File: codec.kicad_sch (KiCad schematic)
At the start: 0 parts

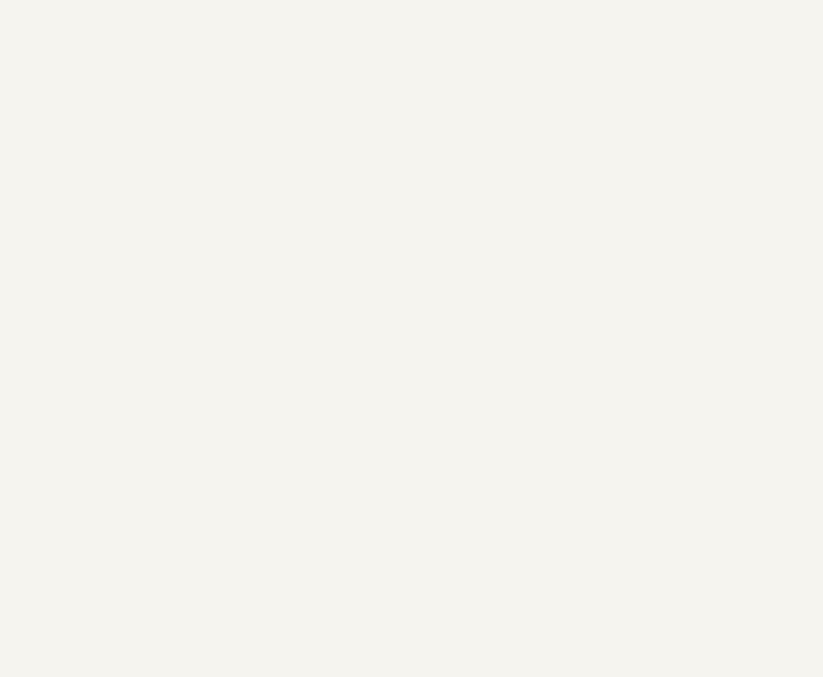
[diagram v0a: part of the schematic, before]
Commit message: Add codec ic
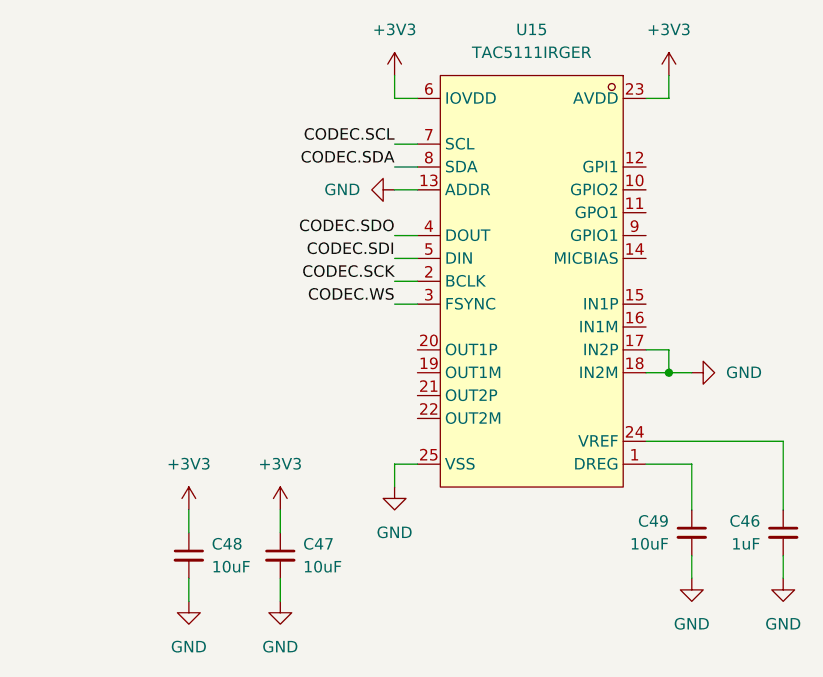
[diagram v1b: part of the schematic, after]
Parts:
- added C46: 1uF, Capacitor_SMD:C_0402_1005Metric, symbol Device:C_Small
- added C47, C48, C49: 10uF, Capacitor_SMD:C_0603_1608Metric, symbol Device:C_Small
- added U15: TAC5111IRGER, custom:VQFN-24_L4.0-W4.0-P0.50-BL-EP2.1_1, symbol custom:TAC5111IRGER
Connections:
- net CODEC.SCK: now also U15.2 (BCLK)
- net CODEC.SCL: now also U15.7 (SCL)
- net CODEC.SDA: now also U15.8 (SDA)
- net CODEC.SDI: now also U15.5 (DIN)
- net CODEC.SDO: now also U15.4 (DOUT)
- net CODEC.WS: now also U15.3 (FSYNC)
- new net: C49.1, U15.1 (DREG)
- new net: C46.1, U15.24 (VREF)
- new net +3V3: C47.1, C48.1, U15.23 (AVDD), U15.6 (IOVDD)
- new net GND: C46.2, C47.2, C48.2, C49.2, U15.13 (ADDR), U15.17 (IN2P), U15.18 (IN2M), U15.25 (VSS), U15.A1 (VSS), U15.A2 (VSS), U15.A3 (VSS), U15.A4 (VSS)

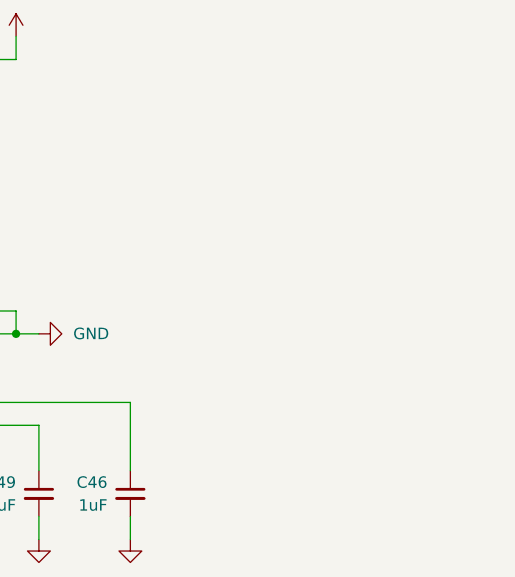
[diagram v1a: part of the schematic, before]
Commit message: Add preamp opamp library
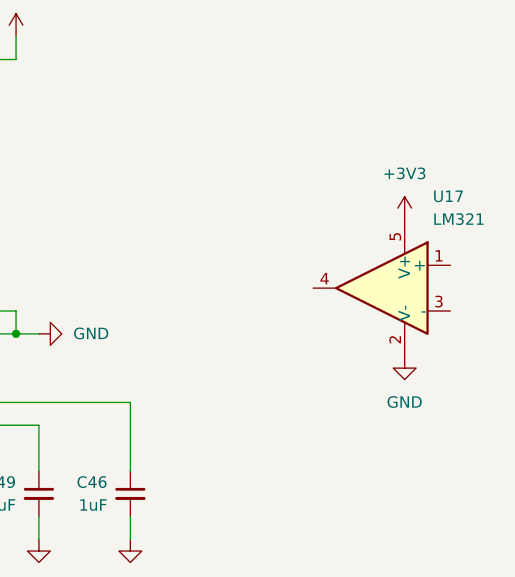
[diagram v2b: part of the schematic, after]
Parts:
- added U17: LM321, custom:SC-70-5_L2.1-W1.3-P0.65-LS2.1-BR, symbol Amplifier_Operational:LM321
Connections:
- net +3V3: now also U17.5 (V+)
- net GND: now also U17.2 (V-)
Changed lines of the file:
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@@
+	)
+	(symbol
+		(lib_id "power:GND")
+		(at 185.42 101.6 0)
+		(mirror y)
+		(unit 1)
+		(body_style 1)
+		(exclude_from_sim no)
+		(in_bom yes)
+		(on_board yes)
+		(in_pos_files yes)
+		(dnp no)
+		(fields_autoplaced yes)
+		(property "Reference" "#PWR0123"
+			(at 185.42 107.95 0)
+			(hide yes)
+			(show_name no)
+			(do_not_autoplace no)
+			(effects
+				(font
+					(size 1.27 1.27)
+				)
+			)
+		)
+		(property "Value" "GND"
+			(at 185.42 106.68 0)
+			(show_name no)
+			(do_not_autoplace no)
+			(effects
+				(font
+					(size 1.27 1.27)
+				)
+			)
+		)
+		(property "Footprint" ""
+			(at 185.42 101.6 0)
+			(hide yes)
+			(show_name no)
+			(do_not_autoplace no)
+			(effects
+				(font
+					(size 1.27 1.27)
+				)
+			)
+		)
+		(property "Datasheet" ""
+			(at 185.42 101.6 0)
+			(hide yes)
+			(show_name no)
+			(do_not_autoplace no)
+			(effects
+				(font
+					(size 1.27 1.27)
+				)
+			)
+		)
+		(property "Description" "Power symbol creates a global label with name \"GND\" , ground"
+			(at 185.42 101.6 0)
+			(hide yes)
+			(show_name no)
+			(do_not_autoplace no)
+			(effects
+				(font
+					(size 1.27 1.27)
+				)
+			)
+		)
+		(pin "1"
+		)
+		(instances
+			(project "pedal"
+				(path "/e2443317-b83f-4e66-ac79-3186c6d613f3/a1bbde72-fd3e-4fef-8e82-ce5db1c82ed5"
+					(reference "#PWR0123")
+					(unit 1)
+				)
+			)
+		)
 	)
 	(symbol
@@
 	)
 	(symbol
+		(lib_id "Amplifier_Operational:LM321")
+		(at 182.88 93.98 0)
+		(mirror y)
+		(unit 1)
+		(body_style 1)
+		(exclude_from_sim no)
+		(in_bom yes)
+		(on_board yes)
+		(in_pos_files yes)
+		(dnp no)
+		(fields_autoplaced yes)
+		(property "Reference" "U17"
+			(at 188.5381 83.82 0)
+			(show_name no)
+			(do_not_autoplace no)
+			(effects
+				(font
+					(size 1.27 1.27)
+				)
+				(justify right)
+			)
+		)
+		(property "Value" "LM321"
+			(at 188.5381 86.36 0)
+			(show_name no)
+			(do_not_autoplace no)
+			(effects
+				(font
+					(size 1.27 1.27)
+				)
+				(justify right)
+			)
+		)
+		(property "Footprint" "custom:SC-70-5_L2.1-W1.3-P0.65-LS2.1-BR"
+			(at 182.88 93.98 0)
+			(hide yes)
+			(show_name no)
+			(do_not_autoplace no)
+			(effects
+				(font
+					(size 1.27 1.27)
+				)
+			)
+		)
+		(property "Datasheet" "http://www.ti.com/lit/ds/symlink/lm321.pdf"
+			(at 182.88 93.98 0)
+			(hide yes)
+			(show_name no)
+			(do_not_autoplace no)
+			(effects
+				(font
+					(size 1.27 1.27)
+				)
+			)
+		)
+		(property "Description" "Low Power Single Operational Amplifier, SOT-23-5"
+			(at 182.88 93.98 0)
+			(hide yes)
+			(show_name no)
+			(do_not_autoplace no)
+			(effects
+				(font
+					(size 1.27 1.27)
+				)
+			)
+		)
+		(pin "2"
+		)
+		(pin "4"
+		)
+		(pin "1"
+		)
+		(pin "3"
+		)
+		(pin "5"
+		)
+		(instances
+			(project "pedal"
+				(path "/e2443317-b83f-4e66-ac79-3186c6d613f3/a1bbde72-fd3e-4fef-8e82-ce5db1c82ed5"
+					(reference "U17")
+					(unit 1)
+				)
+			)
+		)
+	)
+	(symbol
 		(lib_id "power:GND")
 		(at 144.78 99.06 90)
@@
 					(unit 1)
 				)
+			)
+		)
+	)
+	(symbol
+		(lib_id "power:+3V3")
+		(at 185.42 86.36 0)
+		(mirror y)
+		(unit 1)
+		(body_style 1)
+		(exclude_from_sim no)
+		(in_bom yes)
+		(on_board yes)
+		(in_pos_files yes)
+		(dnp no)
+		(fields_autoplaced yes)
+		(property "Reference" "#PWR0121"
+			(at 185.42 90.17 0)
+			(hide yes)
+			(show_name no)
+			(do_not_autoplace no)
+			(effects
+				(font
+					(size 1.27 1.27)
+				)
+			)
+		)
+		(property "Value" "+3V3"
+			(at 185.42 81.28 0)
+			(show_name no)
+			(do_not_autoplace no)
+			(effects
+				(font
+					(size 1.27 1.27)
+				)
+			)
+		)
+		(property "Footprint" ""
+			(at 185.42 86.36 0)
+			(hide yes)
+			(show_name no)
+			(do_not_autoplace no)
+			(effects
+				(font
+					(size 1.27 1.27)
+				)
+			)
+		)
+		(property "Datasheet" ""
+			(at 185.42 86.36 0)
+			(hide yes)
+			(show_name no)
+			(do_not_autoplace no)
+			(effects
+				(font
+					(size 1.27 1.27)
+				)
+			)
+		)
+		(property "Description" "Power symbol creates a global label with name \"+3V3\""
+			(at 185.42 86.36 0)
+			(hide yes)
+			(show_name no)
+			(do_not_autoplace no)
+			(effects
+				(font
+					(size 1.27 1.27)
+				)
+			)
+		)
+		(pin "1"
+		)
+		(instances
+			(project "pedal"
+				(path "/e2443317-b83f-4e66-ac79-3186c6d613f3/a1bbde72-fd3e-4fef-8e82-ce5db1c82ed5"
+					(reference "#PWR0121")
+					(unit 1)
+				)

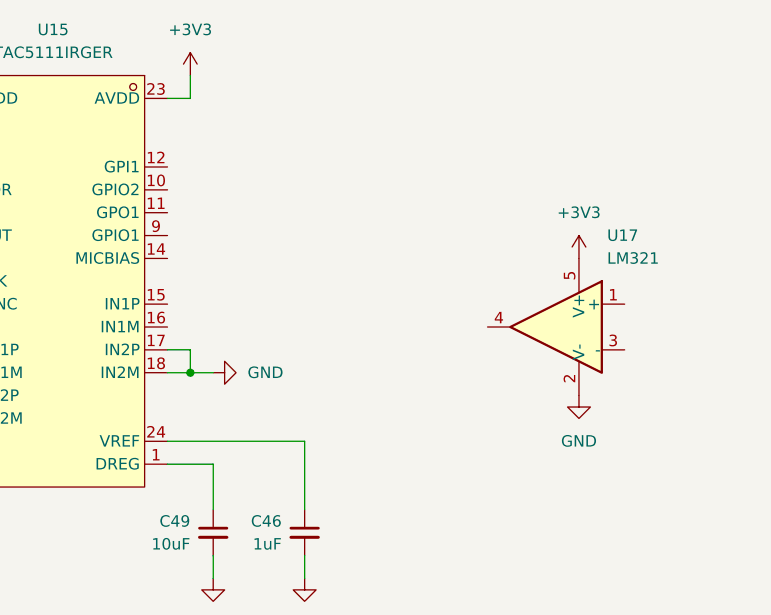
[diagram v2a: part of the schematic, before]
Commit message: Add unity gain preamp
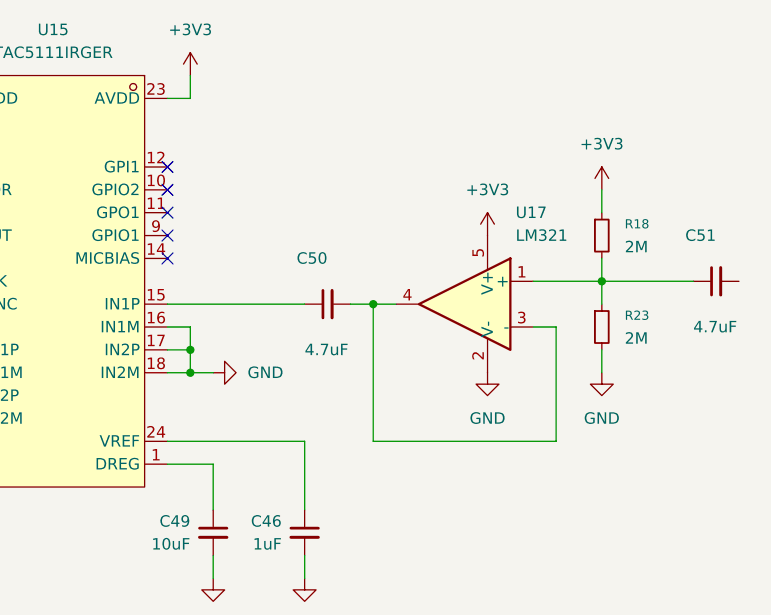
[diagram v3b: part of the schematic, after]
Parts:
- added C50, C51: 4.7uF, Capacitor_SMD:C_0402_1005Metric, symbol Device:C_Small
- added R18, R23: 2M, Resistor_SMD:R_0603_1608Metric, symbol Device:R_Small
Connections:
- net +3V3: now also R18.1
- net GND: now also U15.16 (IN1M), R23.2
- net at U15.15 (IN1P): now also C50.1
- net at U17.1 (+): now also C51.1, R18.2, R23.1
- net at U17.3 (-): now also U17.4, C50.2
- no-connect marks 0 -> 5
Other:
- moved on the sheet: U17

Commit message: Finalize input buffer and filtering
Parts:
- added C53: 10nF, Capacitor_SMD:C_0603_1608Metric, symbol Device:C_Small
- added R24: 0, Resistor_SMD:R_0402_1005Metric, symbol Device:R_Small
- added R25: 680, Resistor_SMD:R_0402_1005Metric, symbol Device:R_Small
- added R26: DNP, Resistor_SMD:R_0402_1005Metric, symbol Device:R_Small
- C50: value 4.7uF -> 330nF; footprint Capacitor_SMD:C_0402_1005Metric -> Resistor_SMD:R_1206_3216Metric; Dielectric (none) -> C0G; LCSC C23733 -> C3837965; Voltage (none) -> 25
- C51: value 4.7uF -> 10nF; footprint Capacitor_SMD:C_0402_1005Metric -> Capacitor_SMD:C_0603_1608Metric; LCSC C23733 -> C76599; Voltage (none) -> 50
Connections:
- net GND: now also C53.2, R26.1
- net at U15.15 (IN1P): now also C50.2; no longer C50.1
- net IN: now reaches C51.2
- new net: R24.1, R26.2, U17.3 (-)
- new net: R24.2, R25.1, U17.4
- new net: C50.1, C53.1, R25.2
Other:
- note added: "HPF using codec input impedance: f_c = 15Hz"
- note added: "HPF: f_c = 15.9Hz"
- note added: "LPF: f_c = 23.4kHz"
- moved on the sheet: C46, C47, C48, C49, R18, R23, U15, U17

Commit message: wip
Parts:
- removed C51: 10nF, Capacitor_SMD:C_0603_1608Metric, symbol Device:C_Small
- removed R25: 680, Resistor_SMD:R_0402_1005Metric, symbol Device:R_Small
- added C52: 1uF, Capacitor_SMD:C_0402_1005Metric, symbol Device:C_Small
- added C54, C55: (no value), Resistor_SMD:R_1206_3216Metric, symbol Device:C_Small
- C53: value 10nF -> 330nF; footprint Capacitor_SMD:C_0603_1608Metric -> Resistor_SMD:R_1206_3216Metric; Dielectric (none) -> C0G; LCSC C76599 -> C3837965; Voltage 50 -> 25
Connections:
- net +3V3: now also C52.2
- net GND: now also U15.21 (OUT2P), U15.22 (OUT2M), C52.1; no longer C53.2
- net IN: now also C53.1
- net at U15.19 (OUT1M): now also C55.2
- net at U15.20 (OUT1P): now also C54.1
- net at R18.2, R23.1, U17.1 (+): now also C53.2
- net at R24.2, U17.4: now also C50.1
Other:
- note added: "HPF using codec input impedance: f_c = 12Hz"
- note added: "HPF: f_c = 0.5Hz"
- note removed: "HPF using codec input impedance: f_c = 15Hz"
- note removed: "HPF: f_c = 15.9Hz"
- note removed: "LPF: f_c = 23.4kHz"
- moved on the sheet: R18, R23, R24, R26, U17

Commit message: Add DirectDrive output amp
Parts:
- added C51, C56, C57: 1uF, Capacitor_SMD:C_0402_1005Metric, symbol Device:C_Small
- added C58, C59, C60, C61: 330nF, Capacitor_SMD:C_1206_3216Metric, symbol Device:C_Small
- added R28, R29, R30, R31, R32, R33, R34, R35: 20k, Resistor_SMD:R_0402_1005Metric, symbol Device:R_Small
- added U16: MAX97220AETE+T, custom:QFN-16_L3.0-W3.0-P0.50-BL-EP1.5, symbol custom:MAX97220AETE+T
- C50, C53: footprint Resistor_SMD:R_1206_3216Metric -> Capacitor_SMD:C_1206_3216Metric
- C54, C55: value (none) -> 1uF; footprint Resistor_SMD:R_1206_3216Metric -> Capacitor_SMD:C_0402_1005Metric; Dielectric C0G -> (none); LCSC C3837965 -> C52923; Voltage 25 -> (none); voltage (none) -> 25
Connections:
- net +3V3: now also C54.1, C51.1, U16.1 (PVDD), U16.13 (SVDD), U16.16 (~{SHDN}), U16.9 (SVDD)
- net GND: now also C54.2, C51.2, C56.2, C57.2, C60.1, C61.1, R29.1, R30.2, U16.17 (EP), U16.3 (PGND), U16.6 (SGND)
- net at U15.19 (OUT1M): now also C59.1; no longer C55.2
- net at U15.20 (OUT1P): now also C58.1; no longer C54.1
- net at C55.1: now also U16.2 (C1P)
- new net: R34.2, R35.1, U16.14 (INL-)
- new net: C61.2, R33.1
- new net: C59.2, R31.1
- new net: R30.1, R31.2, U16.7 (INR+)
- new net: C60.2, R34.1
- new net: C57.1, U16.11 (BIAS)
- new net: R28.2, R29.2, U16.15 (INL+)
- new net: C55.2, U16.4 (C1N)
- new net: C56.1, U16.5 (PVSS)
- new net: R32.2, R33.2, U16.8 (INR-)
- new net: C58.2, R28.1
- new net OUTL: R35.2, U16.12 (OUTL)
- new net OUTR: R32.1, U16.10 (OUTR)
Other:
- note added: "Outputs configured as single-ended, AC coupling caps needed"

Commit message: Replace output amp with TPA6130A2
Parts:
- removed C57: 1uF, Capacitor_SMD:C_0402_1005Metric, symbol Device:C_Small
- removed R28, R29, R30, R31, R32, R33, R34, R35: 20k, Resistor_SMD:R_0402_1005Metric, symbol Device:R_Small
- removed U16: MAX97220AETE+T, custom:QFN-16_L3.0-W3.0-P0.50-BL-EP1.5, symbol custom:MAX97220AETE+T
- added U18: TPA6130A2RTJR, custom:QFN-20_L4.0-W4.0-P0.5-TL-EP, symbol custom:TPA6130A2RTJR
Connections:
- net +3V3: now also U18.12 (VDD), U18.20 (VDD)
- net GND: now also C55.2, C59.1, U18.10 (GND), U18.13 (GND), U18.19 (GND), U18.21 (EP), U18.3 (GND), U18.9 (GND); no longer C56.2, C61.1
- net at U15.19 (OUT1M): now also C61.1; no longer C59.1
- net at C61.2: now also U18.4 (RIGHTINP)
- net at C59.2: now also U18.5 (RIGHTINM)
- net at C60.2: now also U18.1 (LEFTINM)
- net CPVSS: now reaches C55.1
- net CPVSS: now also U18.15 (CPVSS), U18.16 (CPVSS)
- net at C56.1: now also U18.18 (CPP)
- net at C58.2: now also U18.2 (LEFTINP)
- new net: C56.2, U18.17 (CPN)
- new net AMP.SCL: U18.8 (SCL)
- new net AMP.SDA: U18.7 (SDA)
- new net AMP_nSHUTDOWN: U18.6 (~{SD})
- new net OUT_LEFT: U18.14 (HPLEFT)
- new net OUT_RIGHT: U18.11 (HPRIGHT)
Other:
- moved on the sheet: C51, C52, C54, C58, C59, C60, C61

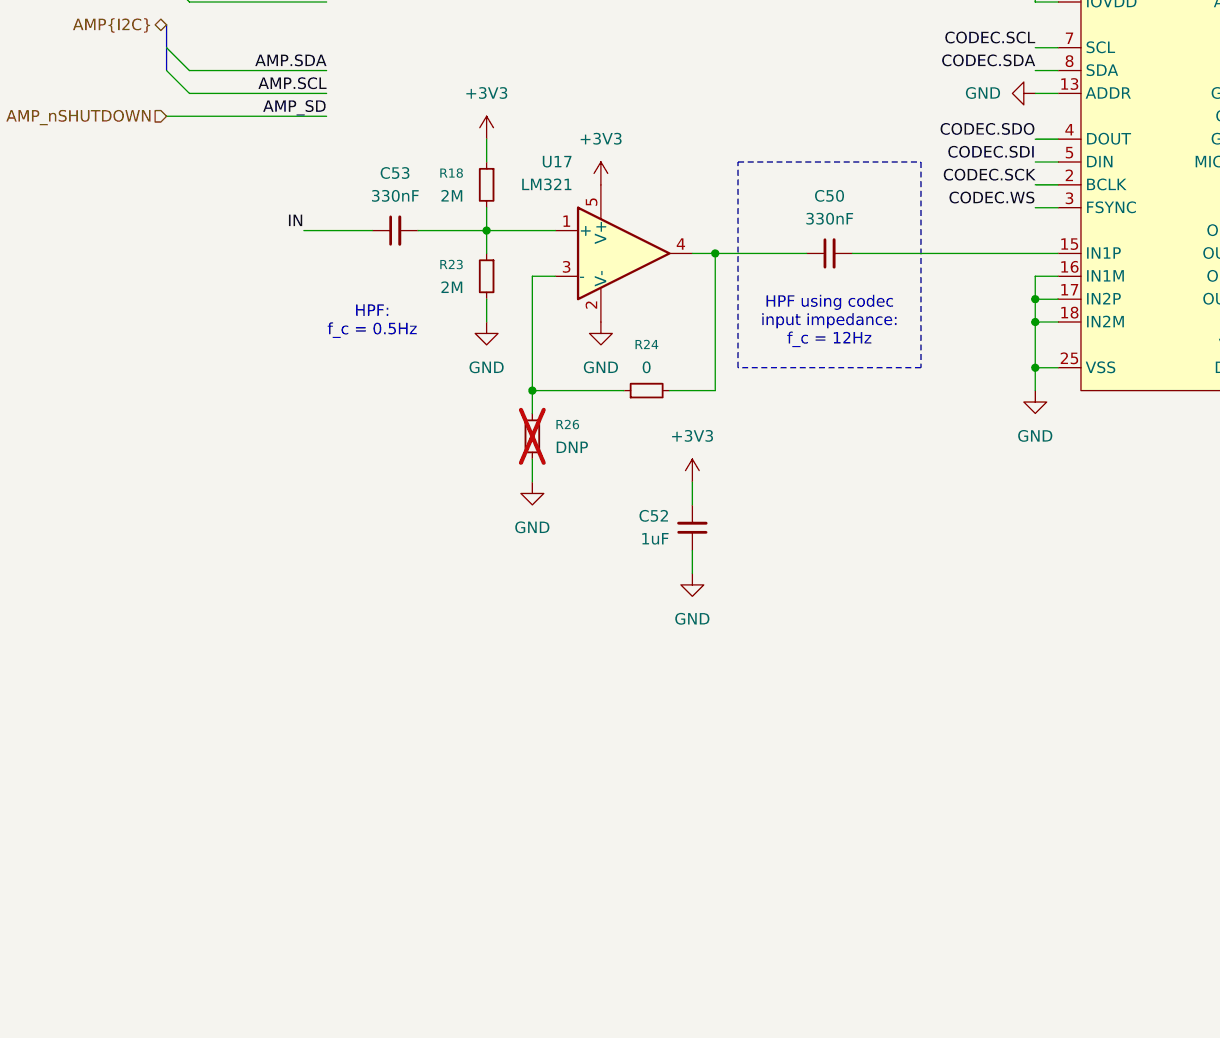
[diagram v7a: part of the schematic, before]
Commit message: Add in/out jacks, remove AC cap at codec input
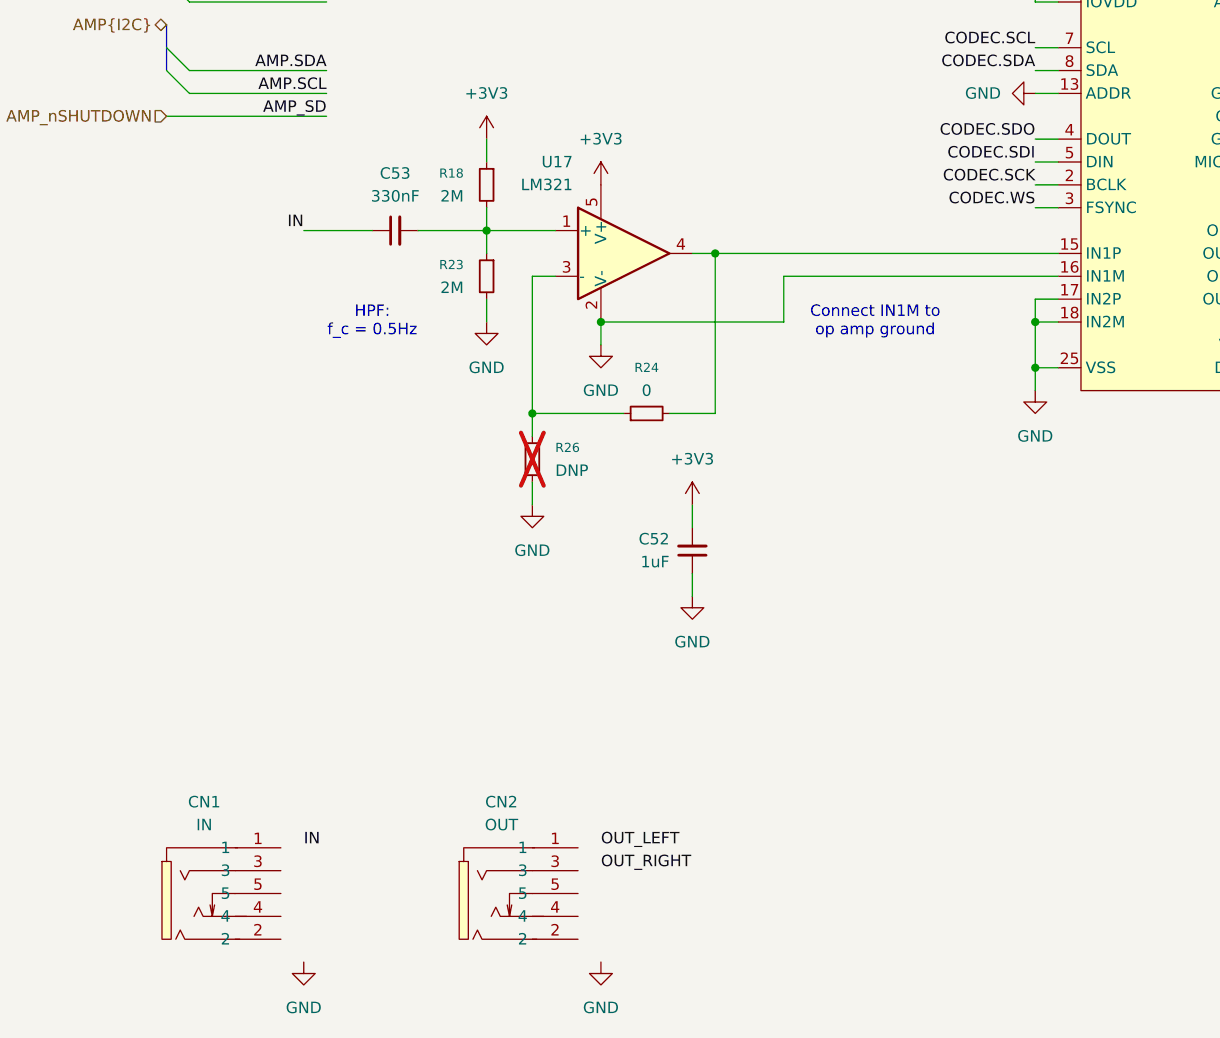
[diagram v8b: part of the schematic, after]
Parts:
- removed C50: 330nF, Capacitor_SMD:C_1206_3216Metric, symbol Device:C_Small
- added CN1: IN, custom:AUDIO-SMD_PJ-3537S, symbol custom:PJ-3537S
- added CN2: OUT, custom:AUDIO-SMD_PJ-3537S, symbol custom:PJ-3537S
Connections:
- net at U15.15 (IN1P): now also R24.2, U17.4
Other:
- note added: "Connect IN1M to op amp ground"
- note removed: "HPF using codec input impedance: f_c = 12Hz"
- moved on the sheet: C52, R24, R26
